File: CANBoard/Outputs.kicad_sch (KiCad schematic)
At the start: 12 parts

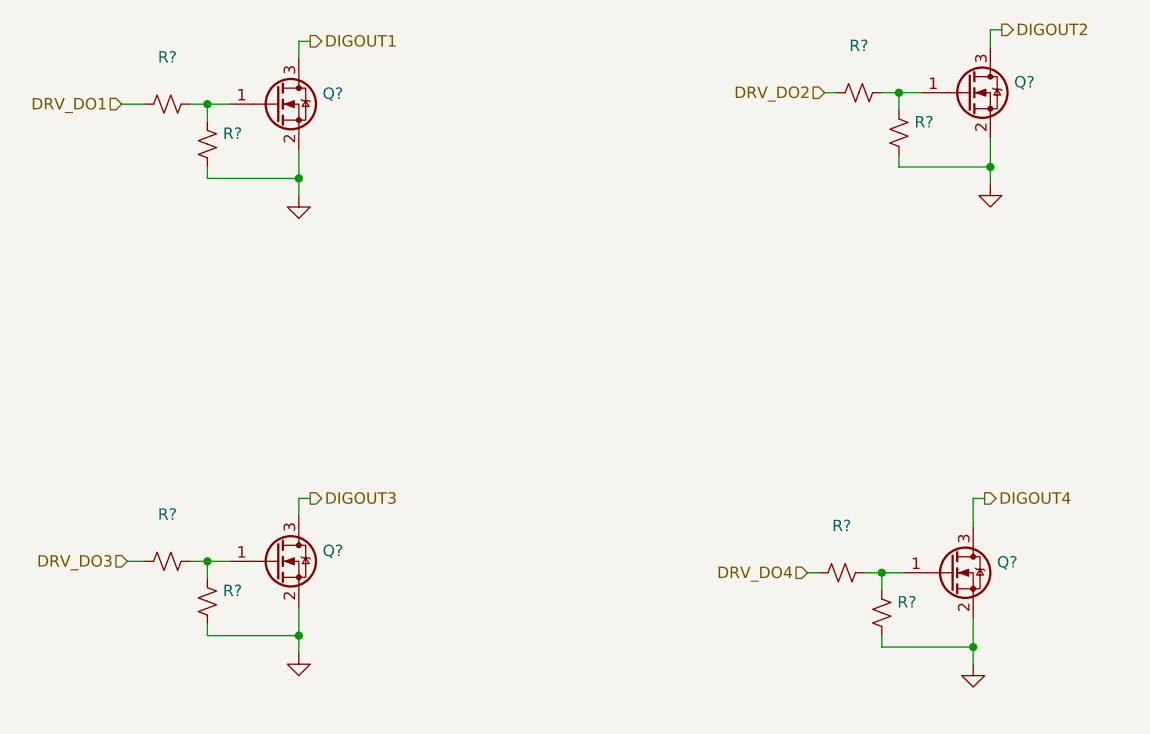
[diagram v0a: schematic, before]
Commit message: V2 updates
Removed FRAM, I2C and SWD pins. Added ID solder jumpers and Tag Connect
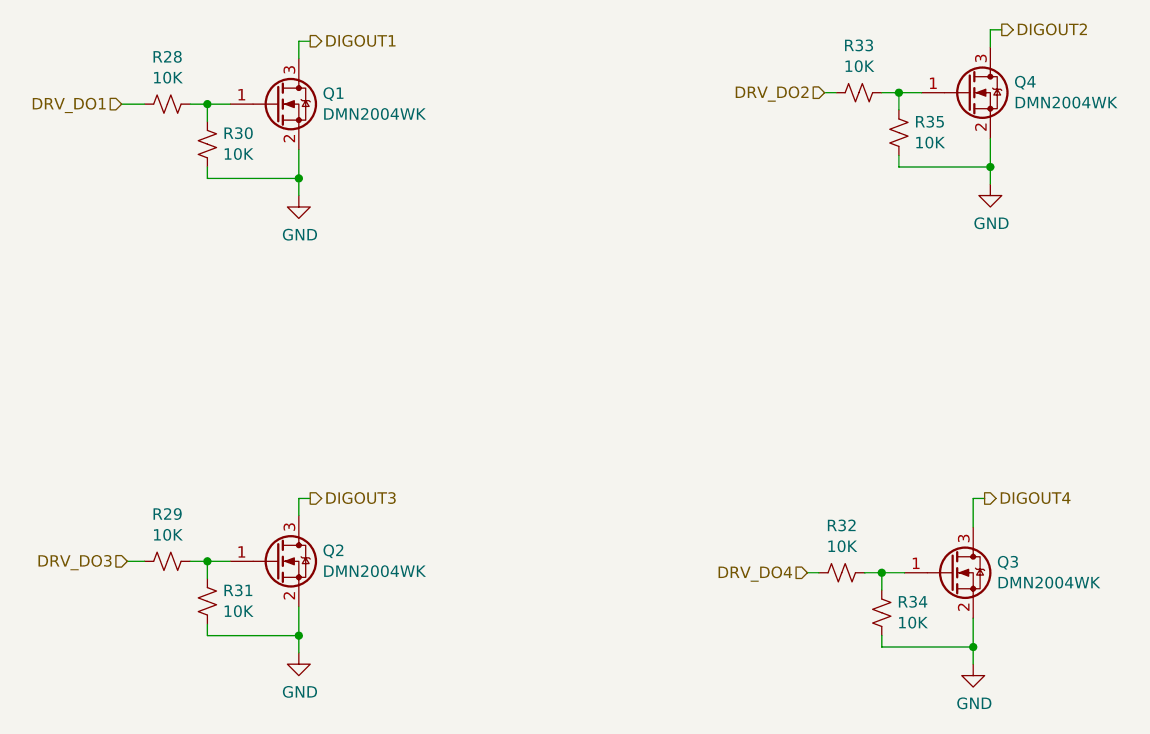
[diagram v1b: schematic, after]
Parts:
- Q1, Q2, Q3, Q4: renamed from Q?; value (none) -> DMN2004WK; footprint (none) -> Package_TO_SOT_SMD:SOT-323_SC-70
- R28, R29, R30, R31, R32, R33, R34, R35: renamed from R?; value (none) -> 10K; footprint (none) -> Resistor_SMD:R_0805_2012Metric

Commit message: Updated outputs, added JLCPCB LCSC part nums
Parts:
- Q1, Q2, Q3, Q4: LCSC (none) -> C151011
- R28, R29, R30, R31, R32, R33, R34, R35: LCSC (none) -> C17414
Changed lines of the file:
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@@
+      (effects (font (size 1.27 1.27)) hide)
+    )
+    (property "LCSC" "C151011" (at 70.485 45.72 0)
       (effects (font (size 1.27 1.27)) hide)
     )
@@
       (effects (font (size 1.27 1.27)) hide)
     )
+    (property "LCSC" "C17414" (at 58.42 45.72 0)
+      (effects (font (size 1.27 1.27)) hide)
+    )
     (pin "1")
     (pin "2")
@@
       (effects (font (size 1.27 1.27)) hide)
     )
+    (property "LCSC" "C17414" (at 62.865 50.165 0)
+      (effects (font (size 1.27 1.27)) hide)
+    )
     (pin "1")
     (pin "2")
@@
       (effects (font (size 1.27 1.27)) hide)
     )
+    (property "LCSC" "C151011" (at 70.485 96.52 0)
+      (effects (font (size 1.27 1.27)) hide)
+    )
     (pin "1")
     (pin "2")
@@
       (effects (font (size 1.27 1.27)) hide)
     )
+    (property "LCSC" "C17414" (at 58.42 96.52 0)
+      (effects (font (size 1.27 1.27)) hide)
+    )
     (pin "1")
     (pin "2")
@@
       (effects (font (size 1.27 1.27)) hide)
     )
+    (property "LCSC" "C17414" (at 62.865 100.965 0)
+      (effects (font (size 1.27 1.27)) hide)
+    )
     (pin "1")
     (pin "2")
@@
       (effects (font (size 1.27 1.27)) hide)
     )
+    (property "LCSC" "C151011" (at 147.32 44.45 0)
+      (effects (font (size 1.27 1.27)) hide)
+    )
     (pin "1")
     (pin "2")
@@
       (effects (font (size 1.27 1.27)) hide)
     )
+    (property "LCSC" "C17414" (at 135.255 44.45 0)
+      (effects (font (size 1.27 1.27)) hide)
+    )
     (pin "1")
     (pin "2")
@@
       (effects (font (size 1.27 1.27)) hide)
     )
+    (property "LCSC" "C17414" (at 139.7 48.895 0)
+      (effects (font (size 1.27 1.27)) hide)
+    )
     (pin "1")
     (pin "2")
@@
       (effects (font (size 1.27 1.27)) hide)
     )
+    (property "LCSC" "C151011" (at 145.415 97.79 0)
+      (effects (font (size 1.27 1.27)) hide)
+    )
     (pin "1")
     (pin "2")
@@
       (effects (font (size 1.27 1.27)) hide)
     )
+    (property "LCSC" "C17414" (at 133.35 97.79 0)
+      (effects (font (size 1.27 1.27)) hide)
+    )
     (pin "1")
     (pin "2")
@@
       (effects (font (size 1.27 1.27)) hide)
     )
+    (property "LCSC" "C17414" (at 137.795 102.235 0)
+      (effects (font (size 1.27 1.27)) hide)
+    )
